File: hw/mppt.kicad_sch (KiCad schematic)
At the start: 11 parts

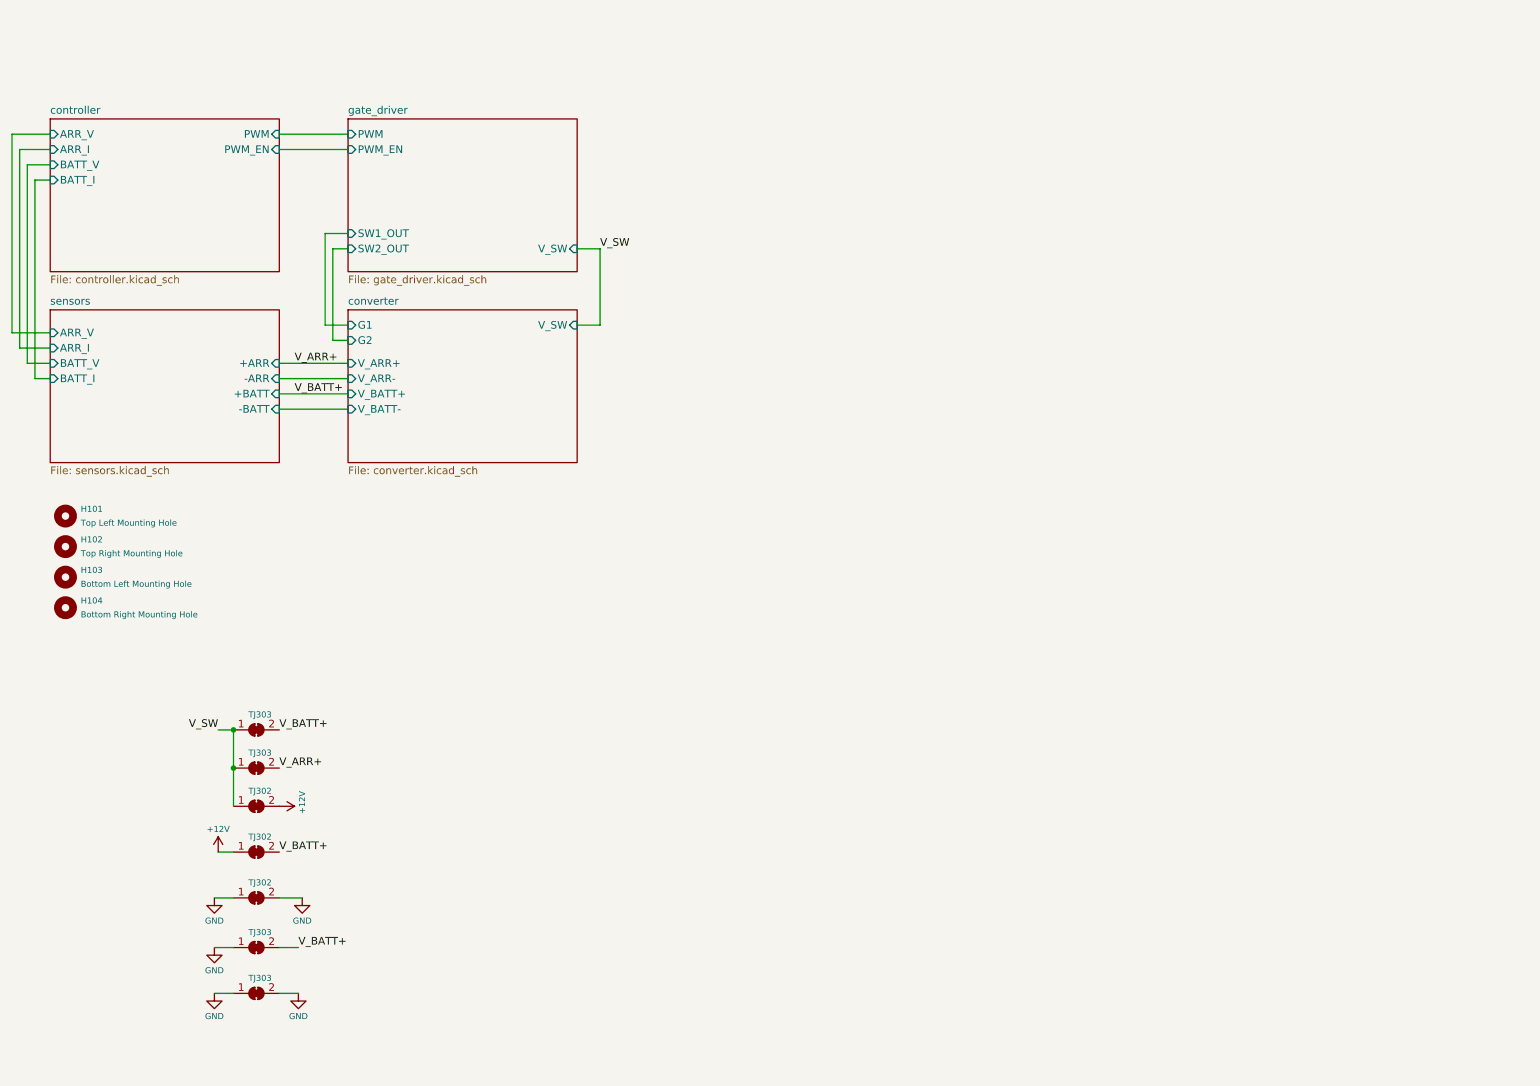
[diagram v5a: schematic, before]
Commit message: fixes for v0.1.1rc
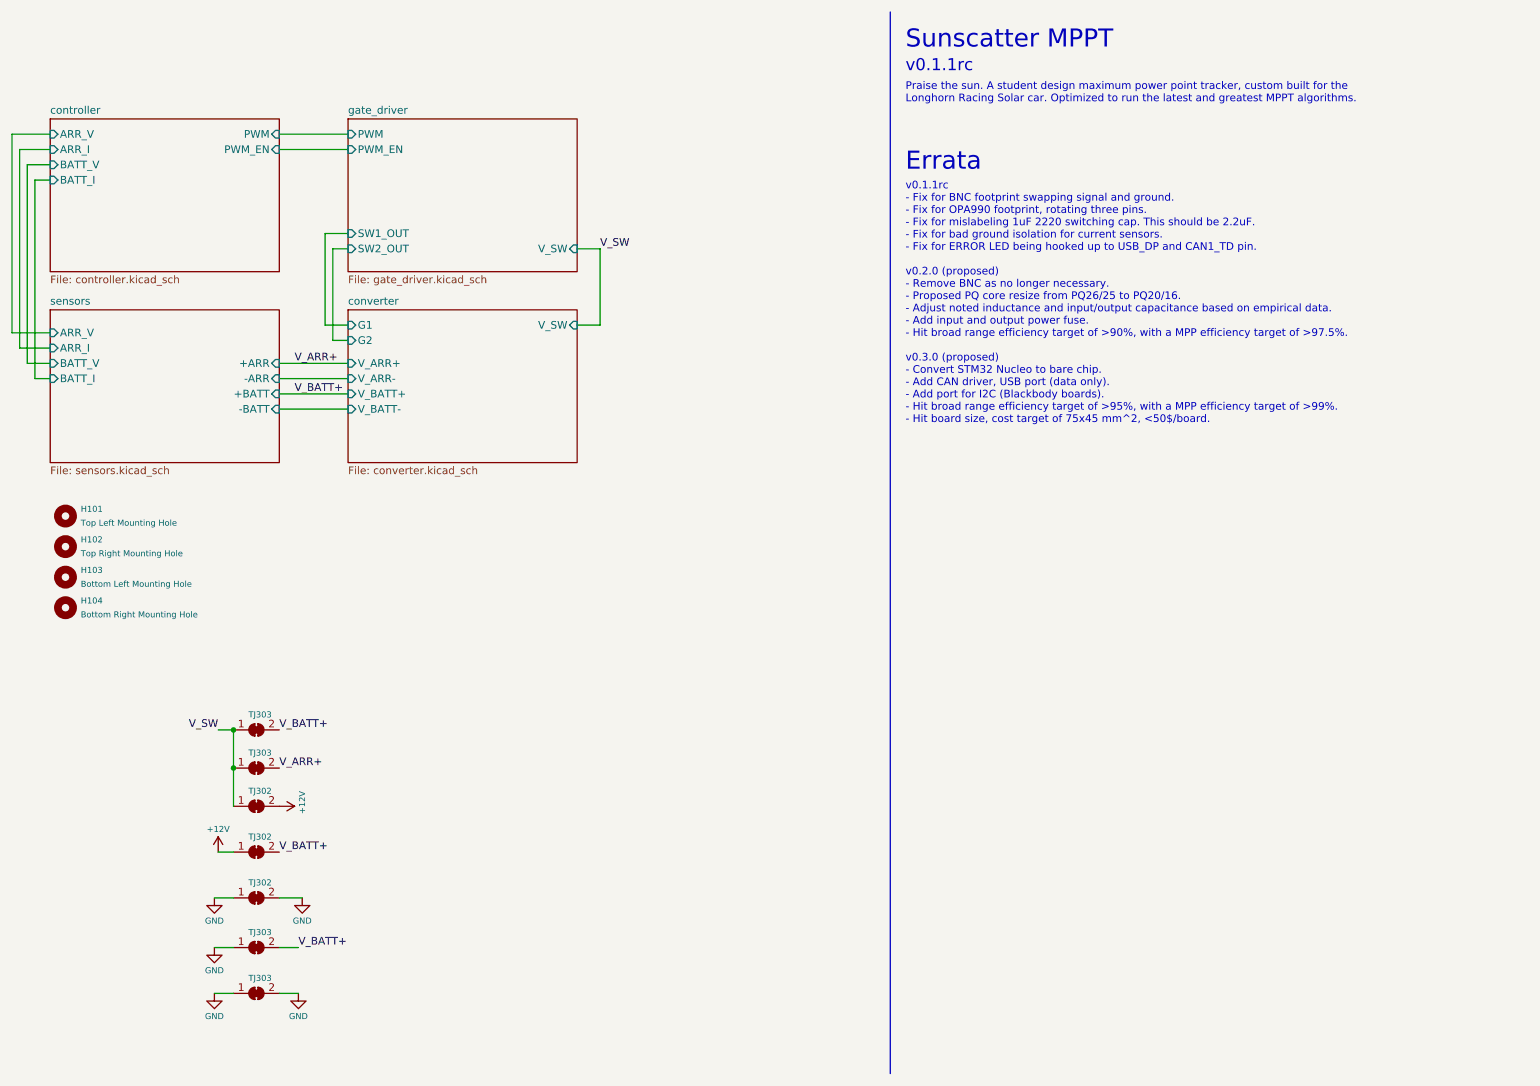
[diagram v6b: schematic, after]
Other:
- note added: "Errata"
- note added: "Praise the sun. A student design maximum power point tracker, custom built for the Longhorn Racing Solar car. Optimized to run the latest and greatest MPPT algorithms."
- note added: "Sunscatter MPPT"
- note added: "v0.1.1rc"
- note added: "v0.1.1rc - Fix for BNC footprint swapping signal and ground. - Fix for OPA990 footprint, rotating three pins. - Fix for mislabeling 1uF 2220 switching cap. This should be 2.2uF. - Fix for bad ground isolation for current sensors. - Fix for ERROR LED being hooked up to USB_DP and CAN1_TD pin. v0.2.0 (proposed) - Remove BNC as no longer necessary. - Proposed PQ core resize from PQ26/25 to PQ20/16. 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"
- company: (none) -> UT LHR Solar
- title: MPPT -> Sunscatter MPPT
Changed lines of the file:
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@@
   (paper "A4")
   (title_block
-    (title "MPPT")
-    (date "2023-01-30")
-    (rev "v0.0.0")
-    (comment 1 "Nishant Gupta")
+    (title "Sunscatter MPPT")
+    (date "2023-03-26")
+    (rev "v0.1.1")
+    (company "UT LHR Solar")
+    (comment 1 "Matthew Yu")
     (comment 2 "Jacob Pustilnik")
     (comment 3 "Matthew Yu")
@@
   )
   (wire (pts (xy 61.595 180.975) (xy 64.77 180.975))
+    (stroke (width 0) (type default))
+  )
+  (polyline (pts (xy 173.99 17.78) (xy 173.99 194.31))
     (stroke (width 0) (type default))
   )
@@
     (stroke (width 0) (type default))
   )
+  (text "Praise the sun. A student design maximum power point tracker, custom built for the \nLonghorn Racing Solar car. Optimized to run the latest and greatest MPPT algorithms."
+    (at 176.53 33.02 0)
+    (effects (font (size 1.27 1.27)) (justify left bottom))
+  )
+  (text "Sunscatter MPPT" (at 176.53 24.13 0)
+    (effects (font (size 3 3)) (justify left bottom))
+  )
+  (text "v0.1.1rc\n" (at 176.53 27.94 0)
+    (effects (font (size 2 2)) (justify left bottom))
+  )
+  (text "Errata" (at 176.53 44.45 0)
+    (effects (font (size 3 3)) (justify left bottom))
+  )
+  (text "v0.1.1rc\n- Fix for BNC footprint swapping signal and ground.\n- Fix for OPA990 footprint, rotating three pins.\n- Fix for mislabeling 1uF 2220 switching cap. This should be 2.2uF.\n- Fix for bad ground isolation for current sensors.\n- Fix for ERROR LED being hooked up to USB_DP and CAN1_TD pin.\n\nv0.2.0 (proposed)\n- Remove BNC as no longer necessary.\n- Proposed PQ core resize from PQ26/25 to PQ20/16.\n- Adjust noted inductance and input/output capacitance based on empirical data.\n- Add input and output power fuse.\n- Hit broad range efficiency target of >90%, with a MPP efficiency target of >97.5%.\n\nv0.3.0 (proposed)\n- Convert STM32 Nucleo to bare chip.\n- Add CAN driver, USB port (data only).\n- Add port for I2C (Blackbody boards).\n- Hit broad range efficiency target of >95%, with a MPP efficiency target of >99%.\n- Hit board size, cost target of 75x45 mm^2, <50$/board."
+    (at 176.53 86.36 0)
+    (effects (font (size 1.27 1.27)) (justify left bottom))
+  )
   (label "V_BATT+" (at 75.565 173.355 0) (fields_autoplaced)
